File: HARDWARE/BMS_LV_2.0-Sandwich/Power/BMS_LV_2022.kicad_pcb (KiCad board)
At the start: 4 copper layers, 90 x 45 mm, 104 parts, among them J1 Conn_01x26, J11 Conn_01x07_Female, J2 AS214-97PN, J4 Battery+, J5 Battery-, Q1 BC846, Q10 BSS138, Q12 SIR5607DP-T1-RE3, Q13 SIR5607DP-T1-RE3, Q14 SIR5607DP-T1-RE3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

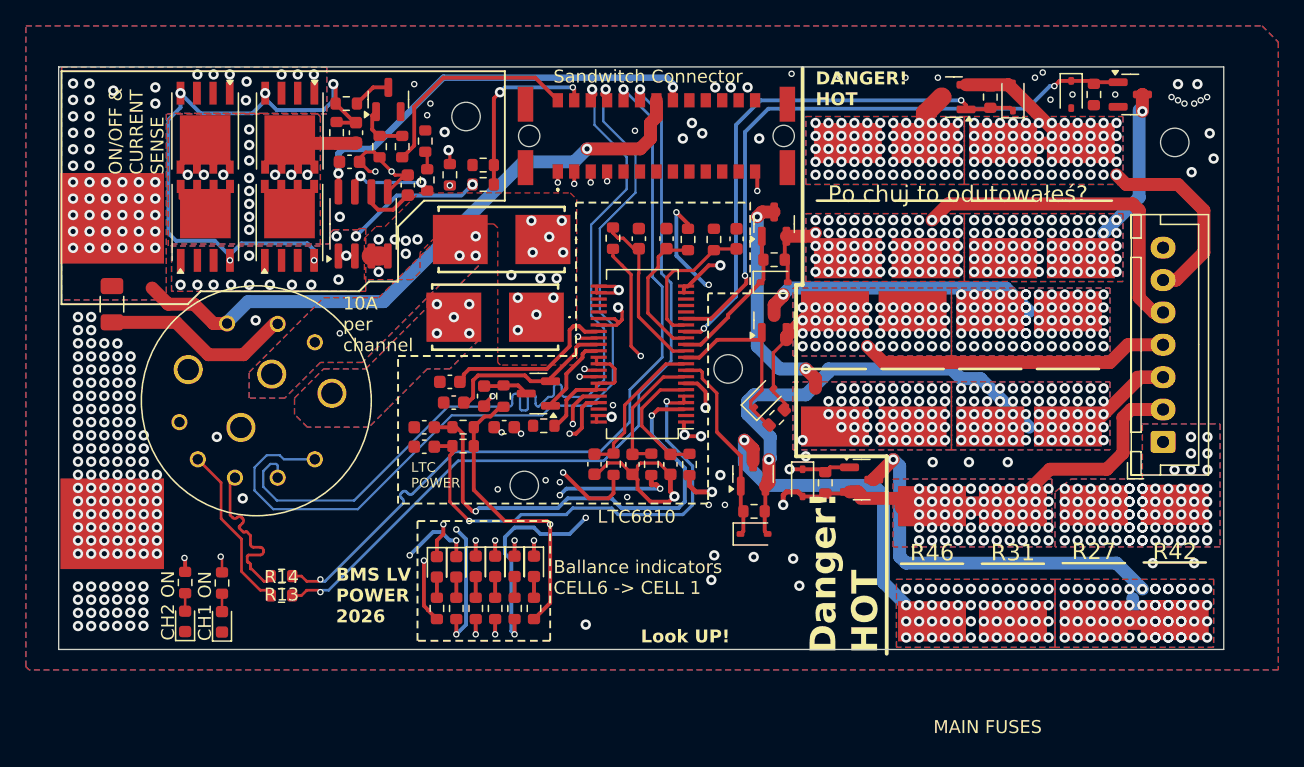
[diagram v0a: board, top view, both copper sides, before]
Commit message: Naprawiono: załączanie lv, brak zlącza programatora (XD) oraz brak podłączenia czujnika prądu :9
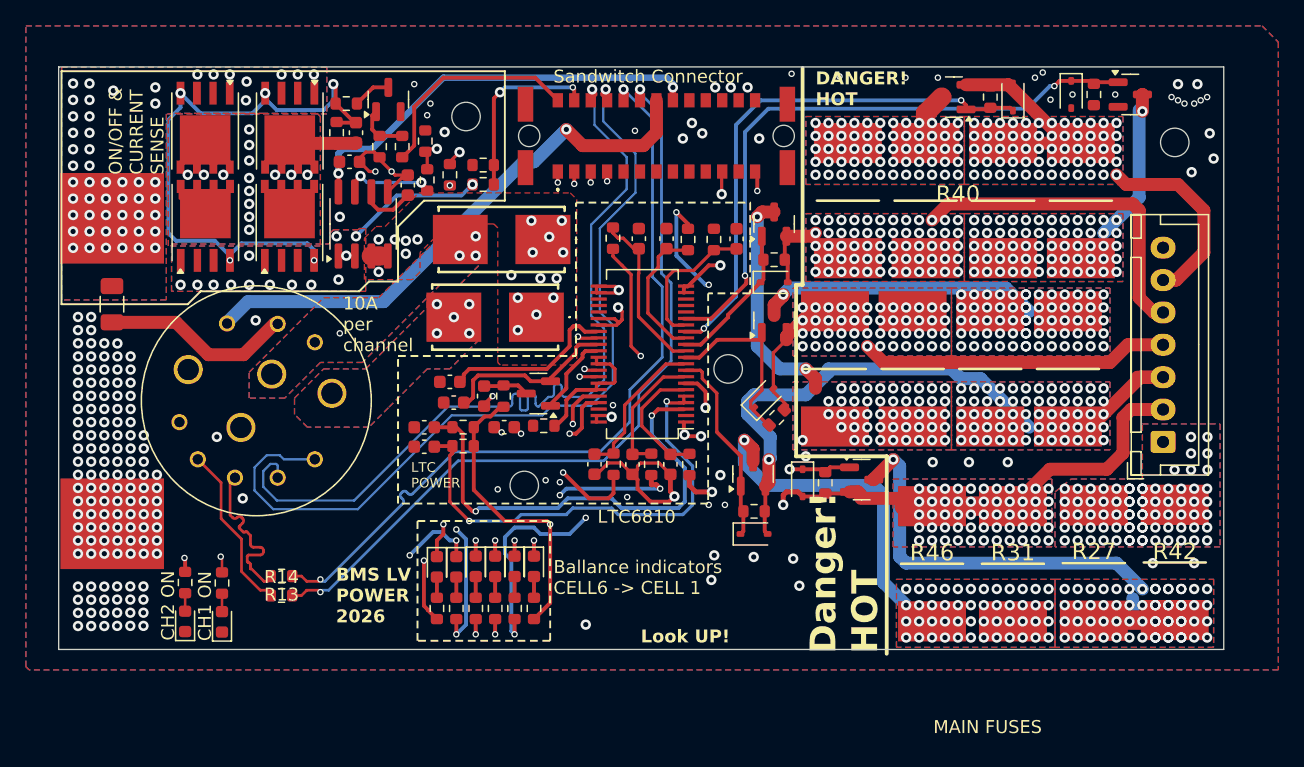
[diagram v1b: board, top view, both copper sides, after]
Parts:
- R40: renamed from Po chuj to odutowałeś?
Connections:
- J1 pad 11: unconnected-(J1-Pin_11-Pad11) -> /CurrentSensor_Out
- J1 pad 20: VCC -> +24V
- J2 pad F: VCC -> +24V
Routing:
- net VCC: track 48.7 -> 0.00 mm, vias 54 -> 53
- net +24V: track 0.00 -> 42.8 mm, vias 0 -> 1
- net /CurrentSensor_Out: track 1.20 -> 28.4 mm, vias 0 -> 2

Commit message: Poprawki , tvs , programator
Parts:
- moved Q15 9.89 mm to (126.4, 84.2), turned to 90 degrees
- moved Q12 9.84 mm to (122.8, 92.7), turned to -90 degrees
- moved Q13 9.35 mm to (132.4, 84.2), turned to 90 degrees
- moved Q14 9.34 mm to (116.8, 92.6), turned to -90 degrees
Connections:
- C41 pad 2: Net-(Q12-S) -> Net-(Q12-D)
- Q12 pad 2: /CS_IP+ -> Net-(Q12-D)
- Q12 pad 3: Net-(Q12-S) -> /CS_IP+
- Q13 pad 2: VCC -> Net-(Q12-D)
- Q13 pad 3: Net-(Q12-S) -> VCC
- Q14 pad 2: /CS_IP+ -> Net-(Q12-D)
- Q14 pad 3: Net-(Q12-S) -> /CS_IP+
- Q15 pad 2: VCC -> Net-(Q12-D)
- Q15 pad 3: Net-(Q12-S) -> VCC
- R62 pad 1: Net-(Q12-S) -> Net-(Q12-D)
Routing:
- net /eFuse/Gate: track 46.2 -> 34.1 mm
- net Net-(Q12-D): track 0.00 -> 5.96 mm, vias 0 -> 8
- net Net-(Q12-S): track 5.45 -> 0.00 mm, vias 14 -> 0
- net /CS_IP+: track 10.7 -> 10.9 mm, vias 14 -> 17
- net VCC: vias 53 -> 55
- net GND: vias 195 -> 194
- added copper zone on B.Cu, net Net-(Q12-D)
- added copper zone on F.Cu, net Net-(Q12-D)
- added copper zone on In1.Cu, net Net-(Q12-D)
- added copper zone on In2.Cu, net Net-(Q12-D)
- removed copper zone on B.Cu, net Net-(Q12-S)
- removed copper zone on F.Cu, net Net-(Q12-S)
- removed copper zone on In1.Cu, net Net-(Q12-S)
- removed copper zone on In2.Cu, net Net-(Q12-S)

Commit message: Dodane zenery, programator w innym miejscu
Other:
- board text added: "BMS SANDWICH 2026 By Wiktor Krakowski V1.1"
- board text removed: "BMS SANDWICH 2026 By Wiktor Krakowski V1.0"

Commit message: Zmieniono tvs, dodano znowu uart, poprawiono silkscreen, gotowy na release
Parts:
- removed the G*** at (150.0, 101.3)
- added G***: LOGO, footprints:zab2, B.Cu at (147.7, 100.8)
